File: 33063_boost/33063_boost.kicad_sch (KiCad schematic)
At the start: 15 parts, among them J1 Conn_01x02, J2 Conn_01x02, U1 33063

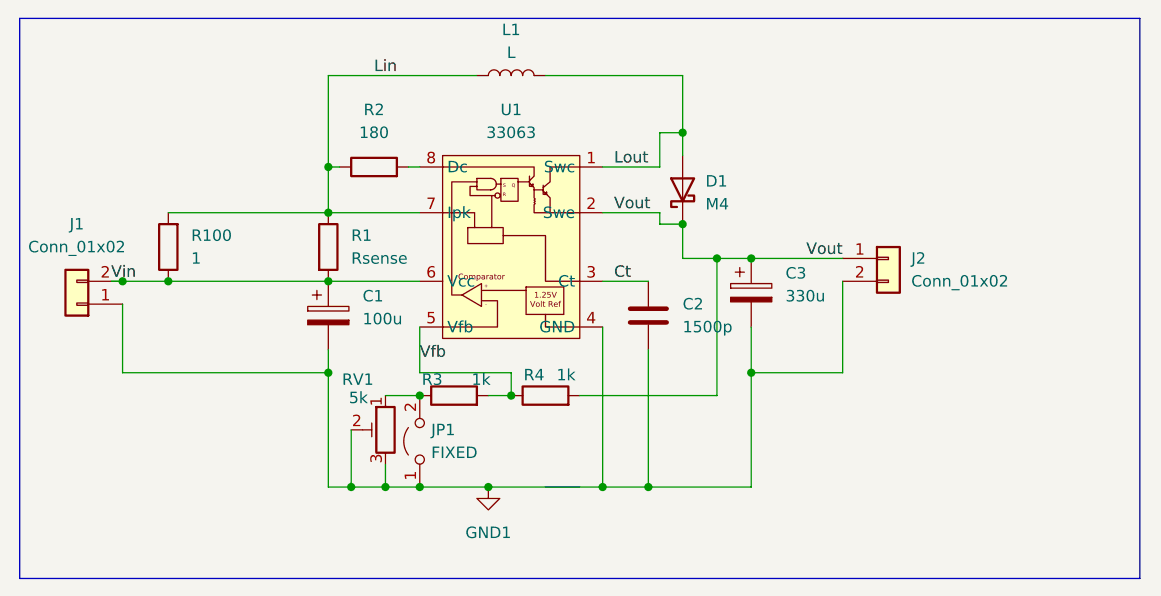
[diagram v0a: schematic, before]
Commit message: added DFN breakout changed trim pot type in 33063_boost, 33063_invert, r1283_power boards fixed error in 33063_boost board (move trim pot to higher side of voltage divider)
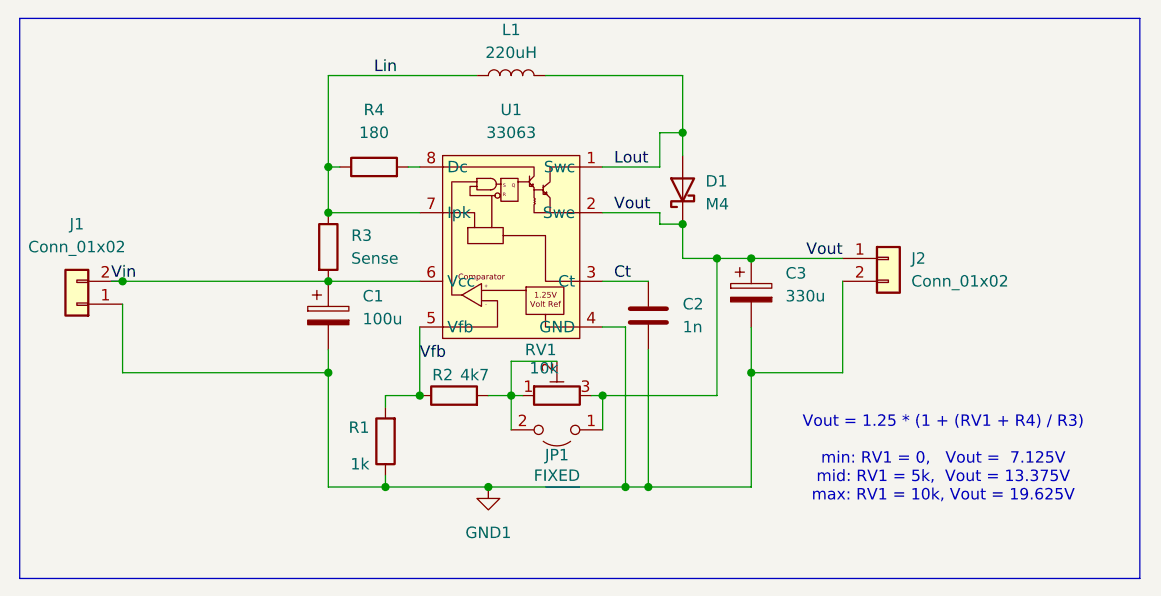
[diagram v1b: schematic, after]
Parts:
- removed R100: 1, misc:0805_5mm, symbol Device:R
- C2: value 1500p -> 1n
- L1: value L -> 220uH
- R2: renamed from R4; value 1k -> 4k7
- R3: renamed from R1; value Rsense -> Sense; footprint Resistor_SMD:R_2512_6332Metric_Pad1.40x3.35mm_HandSolder -> LED_SMD:LED_0805_2012Metric_Pad1.15x1.40mm_HandSolder
- RV1: value 5k -> 10k; footprint misc:trim_pot -> Potentiometer_THT:Potentiometer_Bourns_3296W_Vertical
- renumbered R3 to R1, R2 to R4
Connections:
- net GND1: now also R1.1; no longer JP1.1 (A), RV1.2, RV1.3
- net Vout: now also JP1.1 (A), RV1.3; no longer R2.2
- net at JP1.2 (B), RV1.1: now also R2.2, RV1.2; no longer R1.1
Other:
- note added: "Vout = 1.25 * (1 + (RV1 + R4) / R3) min: RV1 = 0, Vout = 7.125V mid: RV1 = 5k, Vout = 13.375V max: RV1 = 10k, Vout = 19.625V"
- moved on the sheet: JP1, R1, R2, RV1
